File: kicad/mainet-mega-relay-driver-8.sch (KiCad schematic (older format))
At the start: 8 parts, among them J37 Screw_Terminal_01x03, K8 SANYOU_SRD_Form_C, Q8 2N3904, U9 4N37

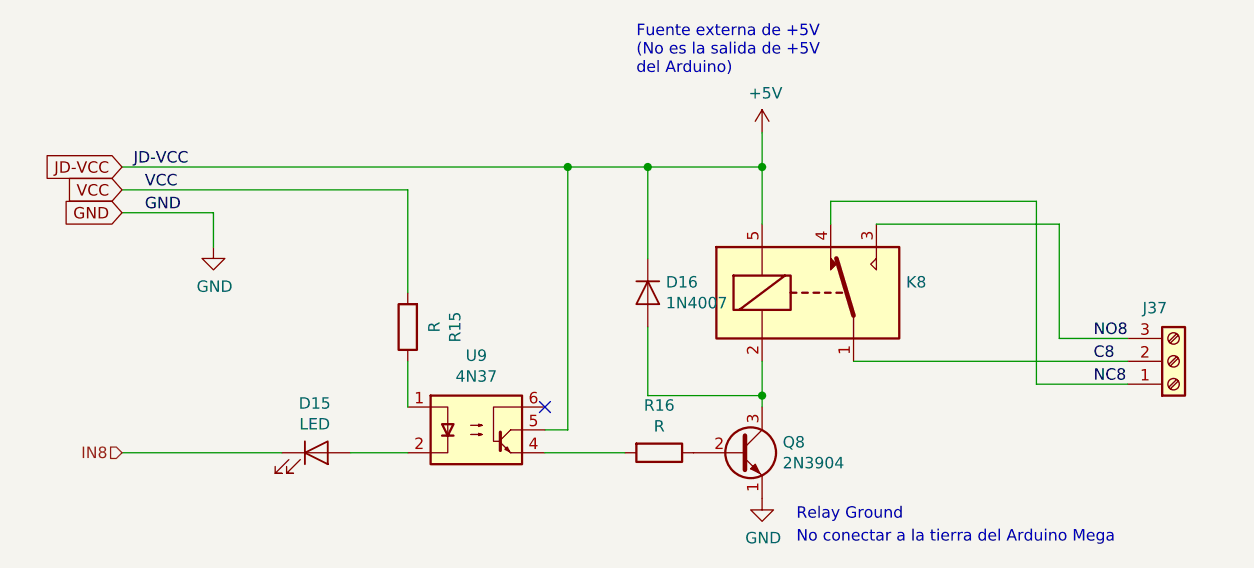
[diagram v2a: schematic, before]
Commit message: KICAD: Actualización de esquematicos del módulo de 8 relés de control
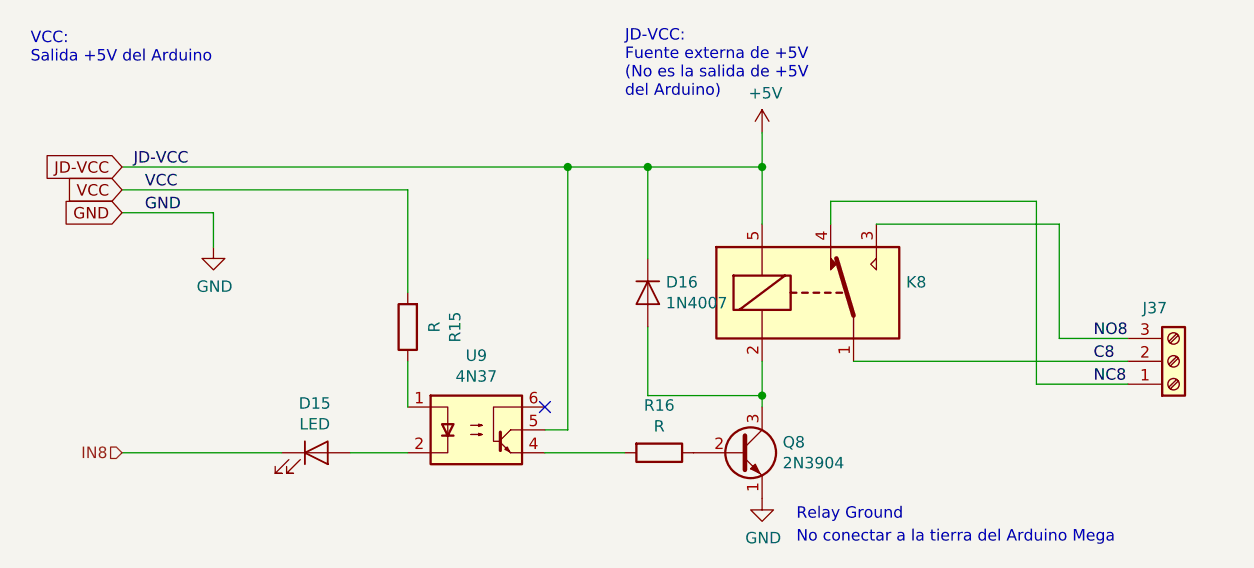
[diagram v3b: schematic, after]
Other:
- note added: "JD-VCC:\nFuente externa de +5V\n(No es la salida de +5V \ndel Arduino)"
- note added: "VCC:\nSalida +5V del Arduino"
- note removed: "Fuente externa de +5V\n(No es la salida de +5V \ndel Arduino)"
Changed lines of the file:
@@
 EESchema Schematic File Version 4
 LIBS:mainet-mega-cache
-LIBS:mainet-mega-5V-to-mp-10v-cache
 EELAYER 30 0
 EELAYER END
 $Descr A4 11693 8268
 encoding utf-8
-Sheet 13 21
-Title ""
-Date ""
+Sheet 14 21
+Title "relay driver 8"
+Date "2021-02-02"
 Rev ""
 Comp ""
@@
 	1    0    0    -1
 $EndComp
-Text Notes 5800 2650 0    50   ~ 0
-Fuente externa de +5V\n(No es la salida de +5V \ndel Arduino)
 Text Notes 6500 4600 0    50   ~ 0
 Relay Ground\n
@@
 Text GLabel 3550 3250 0    50   Input ~ 0
 GND
+Text Notes 5750 2750 0    50   ~ 0
+JD-VCC:\nFuente externa de +5V\n(No es la salida de +5V \ndel Arduino)
+Text Notes 3150 2600 0    50   ~ 0
+VCC:\nSalida +5V del Arduino
 $EndSCHEMATC
